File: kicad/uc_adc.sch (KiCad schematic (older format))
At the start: 6 parts, among them U401 TMS320F28388DZWTS

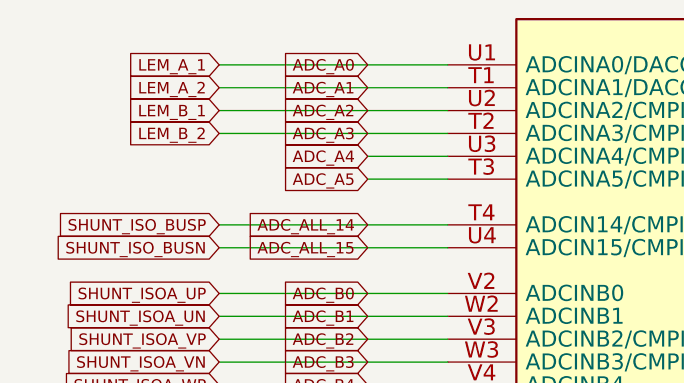
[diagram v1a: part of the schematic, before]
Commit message: I've decided LEM lxs series, it's the best..
I've decided to use the LEM lxs, is a new series better than LTS and is
pin to pin compatible with the old one and also CAS series, so I think
it's a good option. 0.5usec rise time, multi prymari turns options, and
so..
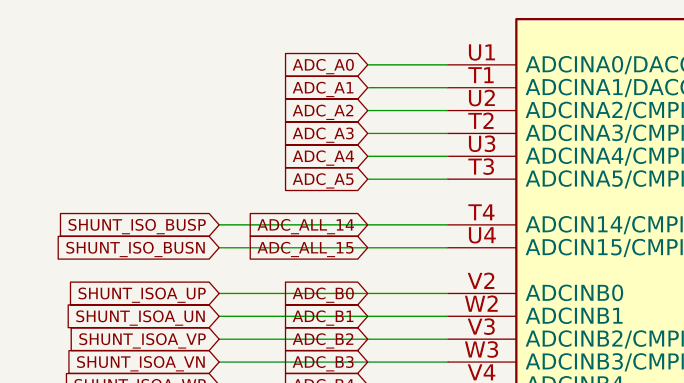
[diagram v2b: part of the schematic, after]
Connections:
- net labels removed: LEM_A_1, LEM_A_2, LEM_B_1, LEM_B_2
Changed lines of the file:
@@
 $Descr A4 11693 8268
 encoding utf-8
-Sheet 3 18
+Sheet 3 19
 Title "ADC"
 Date "25 10 2019"
@@
 Text GLabel 4800 4450 0    50   Input ~ 0
 ADC_D5
-Text GLabel 4150 1850 0    50   Input ~ 0
-LEM_A_2
-Text GLabel 4150 1750 0    50   Input ~ 0
-LEM_A_1
-Wire Wire Line
-	4150 1750 5150 1750
-Wire Wire Line
-	4150 1850 5150 1850
-Text GLabel 4150 1950 0    50   Input ~ 0
-LEM_B_1
-Text GLabel 4150 2050 0    50   Input ~ 0
-LEM_B_2
 Text GLabel 4150 2750 0    50   Input ~ 0
 SHUNT_ISOA_UP
@@
 SHUNT_ISOB_WN
 Wire Wire Line
-	4150 2050 5150 2050
-Wire Wire Line
 	4200 4050 5150 4050
 Wire Wire Line
@@
 $EndComp
 Wire Wire Line
-	4150 1950 5150 1950
-Wire Wire Line
 	5150 2150 4800 2150
 Wire Wire Line
@@
 Wire Wire Line
 	4150 2550 5150 2550
+Wire Wire Line
+	5150 1750 4800 1750
+Wire Wire Line
+	5150 1850 4800 1850
+Wire Wire Line
+	5150 1950 4800 1950
+Wire Wire Line
+	5150 2050 4800 2050
 $EndSCHEMATC

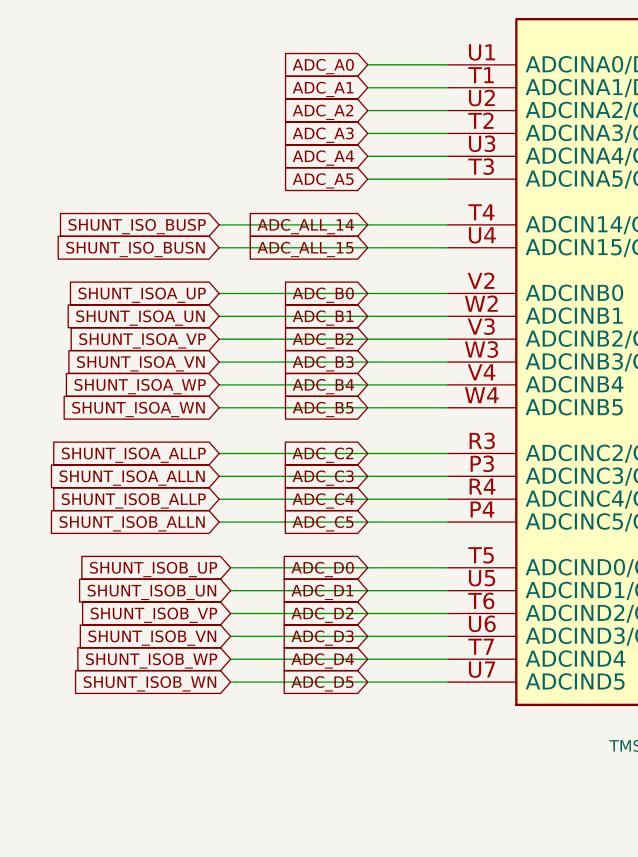
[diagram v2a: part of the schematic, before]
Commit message: I've added LCD UI interfase, EQEP and finish ENDAT
I think I have almos all the interfases ready, I'm begining the
verigication process and then the part definig
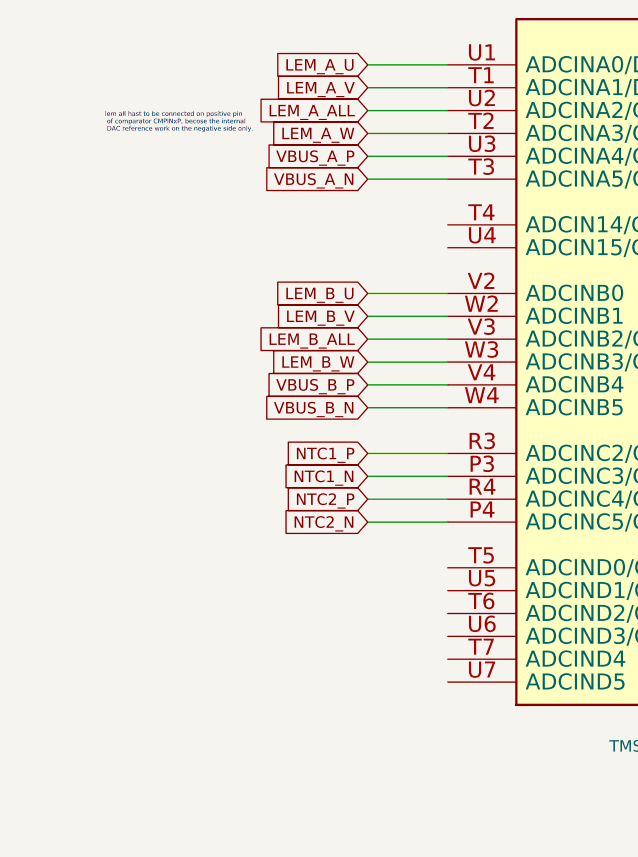
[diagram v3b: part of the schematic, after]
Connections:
- net labels added: LEM_A_ALL, LEM_A_U, LEM_A_V, LEM_A_W, LEM_B_ALL, LEM_B_U, LEM_B_V, LEM_B_W, NTC1_N, NTC1_P, NTC2_N, NTC2_P, VBUS_A_N, VBUS_A_P, VBUS_B_N, VBUS_B_P
- net labels removed: ADC_A0, ADC_A1, ADC_A2, ADC_A3, ADC_A4, ADC_A5, ADC_ALL_14, ADC_ALL_15, ADC_B0, ADC_B1, ADC_B2, ADC_B3, ADC_B4, ADC_B5, ADC_C2, ADC_C3, ADC_C4, ADC_C5, ADC_D0, ADC_D1, ADC_D2, ADC_D3, ADC_D4, ADC_D5, SHUNT_ISOA_ALLN, SHUNT_ISOA_ALLP, SHUNT_ISOA_UN, SHUNT_ISOA_UP, SHUNT_ISOA_VN, SHUNT_ISOA_VP, SHUNT_ISOA_WN, SHUNT_ISOA_WP, SHUNT_ISOB_ALLN, SHUNT_ISOB_ALLP, SHUNT_ISOB_UN, SHUNT_ISOB_UP, SHUNT_ISOB_VN, SHUNT_ISOB_VP, SHUNT_ISOB_WN, SHUNT_ISOB_WP, SHUNT_ISO_BUSN, SHUNT_ISO_BUSP
- wire segments 58 -> 50
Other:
- note added: "lem all hast to be connected on positive pin\n of comparator CMPINxP, becose the internal\n DAC reference work on the negative side only.\n"
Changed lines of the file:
@@
 Wire Wire Line
 	8150 4350 8150 4150
-Text GLabel 4800 1750 0    50   Input ~ 0
-ADC_A0
-Text GLabel 4800 1850 0    50   Input ~ 0
-ADC_A1
-Text GLabel 4800 1950 0    50   Input ~ 0
-ADC_A2
-Text GLabel 4800 2050 0    50   Input ~ 0
-ADC_A3
-Text GLabel 4800 2150 0    50   Input ~ 0
-ADC_A4
-Text GLabel 4800 2250 0    50   Input ~ 0
-ADC_A5
-Text GLabel 4800 2450 0    50   Input ~ 0
-ADC_ALL_14
-Text GLabel 4800 2550 0    50   Input ~ 0
-ADC_ALL_15
-Text GLabel 4800 2750 0    50   Input ~ 0
-ADC_B0
-Text GLabel 4800 2850 0    50   Input ~ 0
-ADC_B1
-Text GLabel 4800 2950 0    50   Input ~ 0
-ADC_B2
-Text GLabel 4800 3050 0    50   Input ~ 0
-ADC_B3
-Text GLabel 4800 3150 0    50   Input ~ 0
-ADC_B4
-Text GLabel 4800 3250 0    50   Input ~ 0
-ADC_B5
-Text GLabel 4800 3450 0    50   Input ~ 0
-ADC_C2
-Text GLabel 4800 3550 0    50   Input ~ 0
-ADC_C3
-Text GLabel 4800 3650 0    50   Input ~ 0
-ADC_C4
-Text GLabel 4800 3750 0    50   Input ~ 0
-ADC_C5
-Text GLabel 4800 3950 0    50   Input ~ 0
-ADC_D0
-Text GLabel 4800 4050 0    50   Input ~ 0
-ADC_D1
-Text GLabel 4800 4150 0    50   Input ~ 0
-ADC_D2
-Text GLabel 4800 4250 0    50   Input ~ 0
-ADC_D3
-Text GLabel 4800 4350 0    50   Input ~ 0
-ADC_D4
-Text GLabel 4800 4450 0    50   Input ~ 0
-ADC_D5
-Text GLabel 4150 2750 0    50   Input ~ 0
-SHUNT_ISOA_UP
-Text GLabel 4150 2850 0    50   Input ~ 0
-SHUNT_ISOA_UN
-Text GLabel 4150 2950 0    50   Input ~ 0
-SHUNT_ISOA_VP
-Text GLabel 4150 3050 0    50   Input ~ 0
-SHUNT_ISOA_VN
-Text GLabel 4150 3150 0    50   Input ~ 0
-SHUNT_ISOA_WP
-Text GLabel 4150 3250 0    50   Input ~ 0
-SHUNT_ISOA_WN
-Text GLabel 4150 2450 0    50   Input ~ 0
-SHUNT_ISO_BUSP
-Text GLabel 4150 2550 0    50   Input ~ 0
-SHUNT_ISO_BUSN
-Text GLabel 4200 3950 0    50   Input ~ 0
-SHUNT_ISOB_UP
-Text GLabel 4200 4050 0    50   Input ~ 0
-SHUNT_ISOB_UN
-Text GLabel 4200 4150 0    50   Input ~ 0
-SHUNT_ISOB_VP
-Text GLabel 4200 4250 0    50   Input ~ 0
-SHUNT_ISOB_VN
-Text GLabel 4200 4350 0    50   Input ~ 0
-SHUNT_ISOB_WP
-Text GLabel 4200 4450 0    50   Input ~ 0
-SHUNT_ISOB_WN
-Wire Wire Line
-	4200 4050 5150 4050
-Wire Wire Line
-	4200 3950 5150 3950
-Wire Wire Line
-	4200 4250 5150 4250
-Wire Wire Line
-	4200 4150 5150 4150
-Wire Wire Line
-	4200 4450 5150 4450
-Wire Wire Line
-	4200 4350 5150 4350
 $Comp
 L servo:TMS320F28388 U401
@@
 	5150 2250 4800 2250
 Wire Wire Line
-	4150 2750 5150 2750
-Wire Wire Line
-	4150 2850 5150 2850
-Wire Wire Line
-	4150 2950 5150 2950
-Wire Wire Line
-	4150 3050 5150 3050
-Wire Wire Line
-	4150 3150 5150 3150
-Wire Wire Line
-	4150 3250 5150 3250
-Text GLabel 4150 3450 0    50   Input ~ 0
-SHUNT_ISOA_ALLP
-Text GLabel 4150 3550 0    50   Input ~ 0
-SHUNT_ISOA_ALLN
-Text GLabel 4150 3650 0    50   Input ~ 0
-SHUNT_ISOB_ALLP
-Text GLabel 4150 3750 0    50   Input ~ 0
-SHUNT_ISOB_ALLN
-Wire Wire Line
-	4150 3650 5150 3650
-Wire Wire Line
-	4150 3750 5150 3750
-Wire Wire Line
-	4150 3550 5150 3550
-Wire Wire Line
-	4150 3450 5150 3450
-Wire Wire Line
-	4150 2450 5150 2450
-Wire Wire Line
-	4150 2550 5150 2550
-Wire Wire Line
 	5150 1750 4800 1750
 Wire Wire Line
@@
 Wire Wire Line
 	5150 2050 4800 2050
+Text GLabel 4800 1750 0    50   Input ~ 0
+LEM_A_U
+Text GLabel 4800 2750 0    50   Input ~ 0
+LEM_B_U
+Text GLabel 4800 1850 0    50   Input ~ 0
+LEM_A_V
+Text GLabel 4800 2850 0    50   Input ~ 0
+LEM_B_V
+Text GLabel 4800 2050 0    50   Input ~ 0
+LEM_A_W
+Text GLabel 4800 3050 0    50   Input ~ 0
+LEM_B_W
+Text GLabel 4800 1950 0    50   Input ~ 0
+LEM_A_ALL
+Text GLabel 4800 2950 0    50   Input ~ 0
+LEM_B_ALL
+Wire Wire Line
+	5150 2750 4800 2750
+Wire Wire Line
+	4800 3050 5150 3050
+Wire Wire Line
+	4800 2950 5150 2950
+Wire Wire Line
+	4800 2850 5150 2850
+Text GLabel 4800 3150 0    50   Input ~ 0
+VBUS_B_P
+Text GLabel 4800 3250 0    50   Input ~ 0
+VBUS_B_N
+Text GLabel 4800 2150 0    50   Input ~ 0
+VBUS_A_P
+Text GLabel 4800 2250 0    50   Input ~ 0
+VBUS_A_N
+Wire Wire Line
+	5150 3150 4800 3150
+Wire Wire Line
+	4800 3250 5150 3250
+Text GLabel 4800 3450 0    50   Input ~ 0
+NTC1_P
+Text GLabel 4800 3550 0    50   Input ~ 0
+NTC1_N
+Text GLabel 4800 3650 0    50   Input ~ 0
+NTC2_P
+Text GLabel 4800 3750 0    50   Input ~ 0
+NTC2_N
+Wire Wire Line
+	4800 3450 5150 3450
+Wire Wire Line
+	4800 3650 5150 3650
+Wire Wire Line
+	4800 3550 5150 3550
+Wire Wire Line
+	4800 3750 5150 3750
+Text Notes 3650 2050 0    20   ~ 0
+lem all hast to be connected on positive pin\n of comparator CMPINxP, becose the internal\n DAC reference work on the negative side only.\n
 $EndSCHEMATC

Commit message: improve ethercat, embedded rj45 to spare, remove some unnecesary r's
I've worked on ethetcat/net to improve visibility on A3 page and also
remove some R's related to leds and change the embedded Rj45 for the
spare transformer and connector 'cause half the price and more options
to choose the connector shape and position
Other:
- note added: "Every interfase to the ADC has the responsability to filter it's output\n before enter ADC pin, for that reason these page just connect to the uC\n without nothin in the middle"
- note added: "uC ADC PINS"
- note removed: "Place near U1"
- moved on the sheet: C429, C432, C433, C436, R436, U401A

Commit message: remove isolation GPIO's and replace it by free pins at IGBT
I remove completely the isolated inputs pins cause I've 8 pins free at
IGBT isolated interfase, so I leave 4 for outpus and 4 for inputs with
one isolated stage, the same as the previous isolated GPIO sheet..
I've improved the DBG sheet and some other details,. I'm ready to make
some electrical checks and fchoose the parts codes and footprints.. go
for it!
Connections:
- net labels added: DACB_DBG_OUT, GND, LCD_AUDIO
- net labels removed: GNDA
- wire segments 50 -> 52
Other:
- note added: "using the DAC out to manage audio \nor other multiporpouse signals"
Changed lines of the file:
@@
 $Descr A3 16535 11693
 encoding utf-8
-Sheet 3 19
+Sheet 3 18
 Title "ADC"
-Date "25 10 2019"
+Date "2020-01-09"
 Rev "1.0"
 Comp "dci"
@@
 Wire Wire Line
 	8200 3450 8600 3450
-$Comp
-L servo:GNDA #PWR?
-U 1 1 5EF6D6BF
-P 7250 5050
-F 0 "#PWR?" H 7250 4800 50  0001 C CNN
-F 1 "GNDA" H 7255 4877 50  0000 C CNN
-F 2 "" H 7250 5050 50  0001 C CNN
-F 3 "" H 7250 5050 50  0001 C CNN
-	1    7250 5050
-	1    0    0    -1
-$EndComp
 Wire Wire Line
 	8600 4850 8200 4850
@@
 $EndComp
 Wire Wire Line
-	4250 2850 3900 2850
-Wire Wire Line
-	4250 2950 3900 2950
-Wire Wire Line
-	4250 2450 3900 2450
-Wire Wire Line
-	4250 2550 3900 2550
-Wire Wire Line
-	4250 2650 3900 2650
-Wire Wire Line
-	4250 2750 3900 2750
-Text GLabel 3900 2450 0    50   Input ~ 0
+	4250 5050 3900 5050
+Wire Wire Line
+	4250 5150 3900 5150
+Wire Wire Line
+	4250 4650 3900 4650
+Wire Wire Line
+	4250 4750 3900 4750
+Wire Wire Line
+	4250 4850 3900 4850
+Wire Wire Line
+	4250 4950 3900 4950
+Text GLabel 3900 4650 0    50   Input ~ 0
 LEM_A_U
 Text GLabel 3900 3450 0    50   Input ~ 0
 LEM_B_U
-Text GLabel 3900 2550 0    50   Input ~ 0
+Text GLabel 3900 4750 0    50   Input ~ 0
 LEM_A_V
 Text GLabel 3900 3550 0    50   Input ~ 0
 LEM_B_V
-Text GLabel 3900 2750 0    50   Input ~ 0
+Text GLabel 3900 4950 0    50   Input ~ 0
 LEM_A_W
 Text GLabel 3900 3750 0    50   Input ~ 0
 LEM_B_W
-Text GLabel 3900 2650 0    50   Input ~ 0
+Text GLabel 3900 4850 0    50   Input ~ 0
 LEM_A_ALL
 Text GLabel 3900 3650 0    50   Input ~ 0
@@
 Text GLabel 3900 3950 0    50   Input ~ 0
 VBUS_B_N
-Text GLabel 3900 2850 0    50   Input ~ 0
+Text GLabel 3900 5050 0    50   Input ~ 0
 VBUS_A_P
-Text GLabel 3900 2950 0    50   Input ~ 0
+Text GLabel 3900 5150 0    50   Input ~ 0
 VBUS_A_N
 Wire Wire Line
@@
 Wire Wire Line
 	3900 4450 4250 4450
-Text Notes 2650 2750 0    20   ~ 0
+Text Notes 2650 4950 0    20   ~ 0
 lem all hast to be connected on positive pin\n of comparator CMPINxP, becose the internal\n DAC reference work on the negative side only.\n
-Text Notes 4250 1050 0    197  ~ 39
+Text Notes 4350 1600 0    197  ~ 39
 uC ADC PINS
-Text Notes 4800 1300 0    20   ~ 0
+Text Notes 4900 1850 0    20   ~ 0
 Every interfase to the ADC has the responsability to filter it's output\n before enter ADC pin, for that reason these page just connect to the uC\n without nothin in the middle
+Text GLabel 3900 2450 0    50   Input ~ 0
+LCD_AUDIO
+Wire Wire Line
+	4250 2450 3900 2450
+Text Notes 3550 2350 0    20   ~ 0
+using the DAC out to manage audio \nor other multiporpouse signals
+Text GLabel 3900 2550 0    50   Input ~ 0
+DACB_DBG_OUT
+Wire Wire Line
+	4250 2550 3900 2550
+$Comp
+L servo:GND #PWR?
+U 1 1 5E9C32E8
+P 7250 5050
+AR Path="/5DCD812E/5E9C32E8" Ref="#PWR?"  Part="1"
+AR Path="/5EAA846A/5E9C32E8" Ref="#PWR?"  Part="1"
+F 0 "#PWR?" H 7255 4901 20  0001 C CNN
+F 1 "GND" H 7255 4849 30  0000 C CNN
+F 2 "" H 7250 5050 70  0000 C CNN
+F 3 "" H 7250 5050 70  0000 C CNN
+	1    7250 5050
+	1    0    0    -1
+$EndComp
 $EndSCHEMATC

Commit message: added 4 push buttons and more gpios on LCD connector
just to have more UI options. With those I'd manage graphics LCD plus 4
buttons, and charaveter LCD. or the embedded EVE graphic LCD
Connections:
- no-connect marks 0 -> 6
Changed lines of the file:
@@
 AR Path="/5DCD812E/5E9C32E8" Ref="#PWR?"  Part="1"
 AR Path="/5EAA846A/5E9C32E8" Ref="#PWR?"  Part="1"
-F 0 "#PWR?" H 7255 4901 20  0001 C CNN
+AR Path="/5DD0E9D6/5E9C32E8" Ref="#PWR0109"  Part="1"
+F 0 "#PWR0109" H 7255 4901 20  0001 C CNN
 F 1 "GND" H 7255 4849 30  0000 C CNN
 F 2 "" H 7250 5050 70  0000 C CNN
@@
 	1    0    0    -1
 $EndComp
+NoConn ~ 4250 2650
+NoConn ~ 4250 2750
+NoConn ~ 4250 2850
+NoConn ~ 4250 2950
+NoConn ~ 4250 3150
+NoConn ~ 4250 3250
 $EndSCHEMATC

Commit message: begin PCB!! it's amess but IT IS
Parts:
- C429, C432, C433, C436: footprint (none) -> Capacitor_SMD:C_0603_1608Metric
- R436: footprint (none) -> Resistor_SMD:R_0603_1608Metric
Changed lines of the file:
@@
 F 0 "C433" V 8350 4400 60  0000 R CNN
 F 1 "2.2uF" V 8150 4400 50  0000 R CNN
-F 2 "" H 8200 4150 50  0001 C CNN
+F 2 "Capacitor_SMD:C_0603_1608Metric" H 8200 4150 50  0001 C CNN
 F 3 "" H 8200 4150 50  0001 C CNN
 F 4 "2.2uF" V -2300 3250 60  0001 C CNN "ValueDisplayed"
@@
 F 0 "C436" V 7645 4040 60  0000 R CNN
 F 1 "1uF" V 7547 4040 50  0000 R CNN
-F 2 "" H 7550 4150 50  0001 C CNN
+F 2 "Capacitor_SMD:C_0603_1608Metric" H 7550 4150 50  0001 C CNN
 F 3 "" H 7550 4150 50  0001 C CNN
 F 4 "1uF" V -6850 3450 60  0001 C CNN "ValueDisplayed"
@@
 F 0 "C429" V 7145 4040 60  0000 R CNN
 F 1 "22uF" V 7047 4040 50  0000 R CNN
-F 2 "" H 7050 4150 50  0001 C CNN
+F 2 "Capacitor_SMD:C_0603_1608Metric" H 7050 4150 50  0001 C CNN
 F 3 "" H 7050 4150 50  0001 C CNN
 F 4 "22uF" V -2350 -1650 60  0001 C CNN "ValueDisplayed"
@@
 F 0 "C432" V 8695 4259 60  0000 L CNN
 F 1 "0.1uF" V 8597 4259 50  0000 L CNN
-F 2 "" H 8600 4150 50  0001 C CNN
+F 2 "Capacitor_SMD:C_0603_1608Metric" H 8600 4150 50  0001 C CNN
 F 3 "" H 8600 4150 50  0001 C CNN
 F 4 "0.1uF" V -1500 3250 60  0001 C CNN "ValueDisplayed"
@@
 F 0 "R436" H 7850 3241 60  0000 C CNN
 F 1 "1k" H 7850 3347 60  0000 C CNN
-F 2 "" H 7850 3450 50  0001 C CNN
+F 2 "Resistor_SMD:R_0603_1608Metric" H 7850 3450 50  0001 C CNN
 F 3 "" H 7850 3450 50  0001 C CNN
 F 4 "" V -2150 650 60  0001 C CNN "ValueDisplayed"

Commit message: I've passed all footprin to layout BUT...
I've passed all, first glance... I need to confirm in details a lot of
things. The objetive for these is to have an aproximation of the size
I'll need to make the board.. then I choose the final detailed footprint
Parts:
- C301: renamed from C429; footprint Capacitor_SMD:C_0603_1608Metric -> servo:C_0603_1608Metric
- C302: renamed from C436; footprint Capacitor_SMD:C_0603_1608Metric -> servo:C_0603_1608Metric
- C303: renamed from C433; footprint Capacitor_SMD:C_0603_1608Metric -> servo:C_0603_1608Metric
- C304: renamed from C432; footprint Capacitor_SMD:C_0603_1608Metric -> servo:C_0603_1608Metric
- U301: renamed from U401; footprint (none) -> servo:BGA337CP80_19X19_1600X1600X140B50N
- renumbered R436 to R301
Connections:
- net NTCA1_N: now reaches U301.T2 (ADCINA3/CMPIN1N)
- net NTCB1_N: now reaches U301.T3 (ADCINA5/CMPIN2N)
- net NTCA1_P: now reaches U301.U2 (ADCINA2/CMPIN1P)
- net NTCB1_P: now reaches U301.U3 (ADCINA4/CMPIN2P)
- net NTC1_N renamed NTCA2_N
- net NTC1_P renamed NTCA2_P
- net NTC2_N renamed NTCB2_N
- net NTC2_P renamed NTCB2_P
- no-connect marks 6 -> 2
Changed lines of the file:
@@
 $Descr A3 16535 11693
 encoding utf-8
-Sheet 3 18
+Sheet 3 19
 Title "ADC"
 Date "2020-01-09"
@@
 Connection ~ 6650 3650
 $Comp
-L servo:Capacitor C433
+L servo:Capacitor C303
 U 1 1 5DB391B8
 P 8200 4150
-F 0 "C433" V 8350 4400 60  0000 R CNN
+F 0 "C303" V 8350 4400 60  0000 R CNN
 F 1 "2.2uF" V 8150 4400 50  0000 R CNN
-F 2 "Capacitor_SMD:C_0603_1608Metric" H 8200 4150 50  0001 C CNN
+F 2 "servo:C_0603_1608Metric" H 8200 4150 50  0001 C CNN
 F 3 "" H 8200 4150 50  0001 C CNN
 F 4 "2.2uF" V -2300 3250 60  0001 C CNN "ValueDisplayed"
@@
 $EndComp
 $Comp
-L servo:Capacitor C436
+L servo:Capacitor C302
 U 1 1 5DB391B3
 P 7550 4150
-F 0 "C436" V 7645 4040 60  0000 R CNN
+F 0 "C302" V 7645 4040 60  0000 R CNN
 F 1 "1uF" V 7547 4040 50  0000 R CNN
-F 2 "Capacitor_SMD:C_0603_1608Metric" H 7550 4150 50  0001 C CNN
+F 2 "servo:C_0603_1608Metric" H 7550 4150 50  0001 C CNN
 F 3 "" H 7550 4150 50  0001 C CNN
 F 4 "1uF" V -6850 3450 60  0001 C CNN "ValueDisplayed"
@@
 $EndComp
 $Comp
-L servo:Capacitor C429
+L servo:Capacitor C301
 U 1 1 5DB3916A
 P 7050 4150
-F 0 "C429" V 7145 4040 60  0000 R CNN
+F 0 "C301" V 7145 4040 60  0000 R CNN
 F 1 "22uF" V 7047 4040 50  0000 R CNN
-F 2 "Capacitor_SMD:C_0603_1608Metric" H 7050 4150 50  0001 C CNN
+F 2 "servo:C_0603_1608Metric" H 7050 4150 50  0001 C CNN
 F 3 "" H 7050 4150 50  0001 C CNN
 F 4 "22uF" V -2350 -1650 60  0001 C CNN "ValueDisplayed"
@@
 $EndComp
 $Comp
-L servo:Capacitor C432
+L servo:Capacitor C304
 U 1 1 5DB39165
 P 8600 4150
-F 0 "C432" V 8695 4259 60  0000 L CNN
+F 0 "C304" V 8695 4259 60  0000 L CNN
 F 1 "0.1uF" V 8597 4259 50  0000 L CNN
-F 2 "Capacitor_SMD:C_0603_1608Metric" H 8600 4150 50  0001 C CNN
+F 2 "servo:C_0603_1608Metric" H 8600 4150 50  0001 C CNN
 F 3 "" H 8600 4150 50  0001 C CNN
 F 4 "0.1uF" V -1500 3250 60  0001 C CNN "ValueDisplayed"
@@
 $EndComp
 $Comp
-L servo:3V3A #PWR0416
+L servo:3V3A #PWR0302
 U 1 1 5E5CB351
 P 8600 3350
-F 0 "#PWR0416" H 8605 3557 20  0001 C CNN
+F 0 "#PWR0302" H 8605 3557 20  0001 C CNN
 F 1 "3V3A" H 8605 3507 28  0000 C CNN
 F 2 "" H 8600 3350 50  0001 C CNN
@@
 	7050 3950 7050 3450
 $Comp
-L servo:Resistor R436
+L servo:Resistor R301
 U 1 1 5E88CCA6
 P 7850 3450
-F 0 "R436" H 7850 3241 60  0000 C CNN
+F 0 "R301" H 7850 3241 60  0000 C CNN
 F 1 "1k" H 7850 3347 60  0000 C CNN
 F 2 "Resistor_SMD:R_0603_1608Metric" H 7850 3450 50  0001 C CNN
@@
 Wire Wire Line
 	7250 5050 7250 4850
-$Comp
-L servo:TMS320F28388 U401
-U 1 1 5DB3916E
-P 5350 3750
-F 0 "U401" H 5350 2167 60  0000 C CNN
-F 1 "TMS320F28388DZWTS" H 5350 2069 50  0000 C CNN
-F 2 "" H 5350 3750 50  0001 C CNN
-F 3 "../doc/datasheets/tms320f28388d_datasheet.pdf" H 5350 3750 50  0001 C CNN
-F 4 "TMS320F28388DZWTS" V -1450 -350 60  0001 C CNN "PartNumber"
-	1    5350 3750
-	1    0    0    -1
-$EndComp
 Wire Wire Line
 	4250 5050 3900 5050
@@
 Wire Wire Line
 	3900 3950 4250 3950
-Text GLabel 3900 4150 0    50   Input ~ 0
-NTC1_P
-Text GLabel 3900 4250 0    50   Input ~ 0
-NTC1_N
 Text GLabel 3900 4350 0    50   Input ~ 0
-NTC2_P
+NTCB2_P
 Text GLabel 3900 4450 0    50   Input ~ 0
-NTC2_N
+NTCB2_N
 Wire Wire Line
 	3900 4150 4250 4150
@@
 AR Path="/5DCD812E/5E9C32E8" Ref="#PWR?"  Part="1"
 AR Path="/5EAA846A/5E9C32E8" Ref="#PWR?"  Part="1"
-AR Path="/5DD0E9D6/5E9C32E8" Ref="#PWR0109"  Part="1"
-F 0 "#PWR0109" H 7255 4901 20  0001 C CNN
+AR Path="/5DD0E9D6/5E9C32E8" Ref="#PWR0301"  Part="1"
+F 0 "#PWR0301" H 7255 4901 20  0001 C CNN
 F 1 "GND" H 7255 4849 30  0000 C CNN
 F 2 "" H 7250 5050 70  0000 C CNN
@@
 	1    0    0    -1
 $EndComp
-NoConn ~ 4250 2650
-NoConn ~ 4250 2750
-NoConn ~ 4250 2850
-NoConn ~ 4250 2950
 NoConn ~ 4250 3150
 NoConn ~ 4250 3250
+Text GLabel 3900 4150 0    50   Input ~ 0
+NTCA2_P
+Text GLabel 3900 4250 0    50   Input ~ 0
+NTCA2_N
+Text GLabel 3900 2850 0    50   Input ~ 0
+NTCB1_P
+Text GLabel 3900 2950 0    50   Input ~ 0
+NTCB1_N
+Text GLabel 3900 2650 0    50   Input ~ 0
+NTCA1_P
+Text GLabel 3900 2750 0    50   Input ~ 0
+NTCA1_N
+$Comp
+L servo:TMS320F28388 U301
+U 1 1 5DB3916E
+P 5350 3750
+F 0 "U301" H 5350 2167 60  0000 C CNN
+F 1 "TMS320F28388DZWTS" H 5350 2069 50  0000 C CNN
+F 2 "servo:BGA337CP80_19X19_1600X1600X140B50N" H 5350 3750 50  0001 C CNN
+F 3 "../doc/datasheets/tms320f28388d_datasheet.pdf" H 5350 3750 50  0001 C CNN
+F 4 "TMS320F28388DZWTS" V -1450 -350 60  0001 C CNN "PartNumber"
+	1    5350 3750
+	1    0    0    -1
+$EndComp
+Wire Wire Line
+	4250 2650 3900 2650
+Wire Wire Line
+	3900 2750 4250 2750
+Wire Wire Line
+	4250 2850 3900 2850
+Wire Wire Line
+	3900 2950 4250 2950
 $EndSCHEMATC
